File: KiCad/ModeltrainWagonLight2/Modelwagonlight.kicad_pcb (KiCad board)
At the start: 2 copper layers, 25 x 11 mm, 17 parts, among them J1 Conn_01x01, J2 Conn_01x01, J3 Conn_01x01, J4 Conn_01x01, U1 LP2951DR

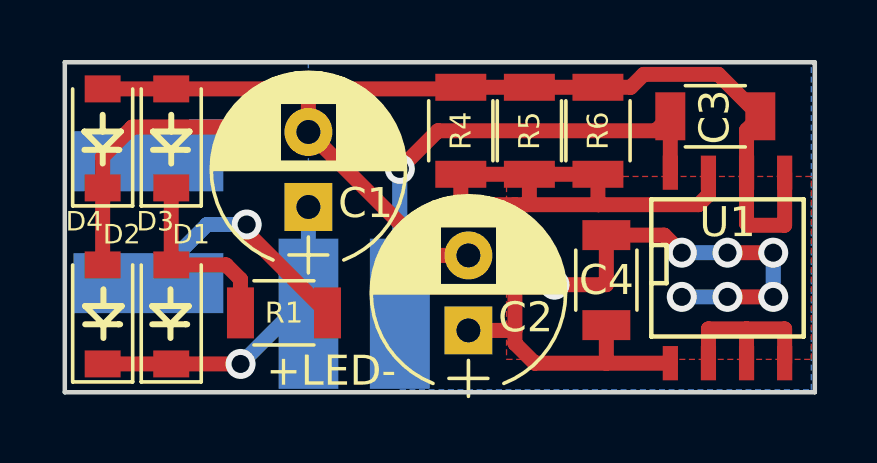
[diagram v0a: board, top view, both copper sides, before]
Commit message: Redrawn Modelwagonlight schematic and layout.
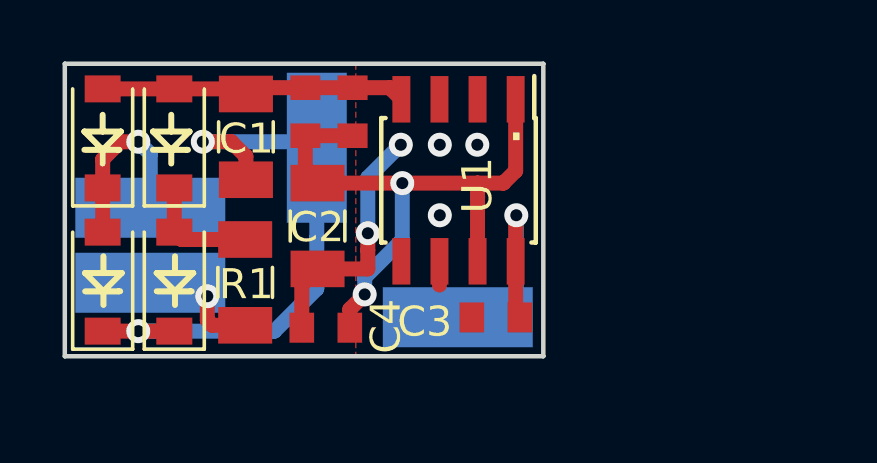
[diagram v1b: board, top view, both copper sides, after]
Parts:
- removed R6: 100R, Resistors_SMD:R_1206
- C1, C2: value 22uF -> 22u; footprint Capacitors_THT:CP_Radial_D6.3mm_P2.50mm -> Capacitor_SMD:C_1206_3216Metric
- C3, C4: value 100nF -> 100n; footprint Capacitors_SMD:C_1206 -> Capacitor_SMD:C_0603_1608Metric
- D1, D2: footprint Diodes_SMD:D_SOD-123 -> Diode_SMD:D_SOD-123
- R1: value 10R -> 47E; footprint Resistors_SMD:R_1206 -> Resistor_SMD:R_1206_3216Metric
- R4: value 100R -> 470E; footprint Resistors_SMD:R_1206 -> Resistor_SMD:R_0603_1608Metric
- R5: value 100R -> NP; footprint Resistors_SMD:R_1206 -> Resistor_SMD:R_0603_1608Metric
- U1: footprint SMD_Packages:SOIC-8-N -> Package_SO:SOIC-8_3.9x4.9mm_P1.27mm
- moved C3 9.92 mm to (204.4, 119.5), turned to 180 degrees
- moved C4 9.49 mm to (198.7, 119.8), turned to 180 degrees
- moved U1 9.43 mm to (203.1, 114.9), turned to 270 degrees
- moved C2 6.12 mm to (198.4, 116.5), turned to 270 degrees
- moved R5 5.93 mm to (199.6, 112.6)
- moved J3 5.54 mm to (198.4, 113.8)
- moved R4 5.22 mm to (198.0, 112.6)
- moved C1 3.13 mm to (196.0, 113.5)
- moved J4 1.94 mm to (203.1, 119.5), turned to 0 degrees
- moved R1 1.64 mm to (196.0, 118.3), turned to 90 degrees
- moved J2 1.55 mm to (192.8, 115.8), turned to 0 degrees
- moved D1 1.10 mm to (193.6, 118.3)
- moved D2 1.09 mm to (191.3, 118.3)
- moved D3 0.10 mm to (193.6, 113.5)
- moved J1 0.07 mm to (192.8, 118.3), turned to 0 degrees
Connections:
- net Net-(C1-Pad2) renamed GND
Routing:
- net GND: track 57.7 -> 19.6 mm, vias 7 -> 5
- net Net-(C2-Pad1): track 30.0 -> 20.7 mm, vias 0 -> 2
- net Net-(C1-Pad1): track 11.1 -> 19.9 mm
- net Net-(C3-Pad1): track 16.4 -> 8.82 mm
- net Net-(D2-Pad2): track 13.0 -> 6.22 mm
- net Net-(J1-Pad1): track 8.15 -> 4.22 mm
- net Net-(D1-Pad2): track 6.19 -> 3.94 mm
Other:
- board size 25 x 11 mm -> 15.9 x 9.8 mm
- board text added: "."
- board text added: "2019"
- board text added: "Jsif"
- board text added: "LED"
- board text added: "V2.0"
- board text added: "Wlight"
- board text added: "^IN^"
- board text removed: "+LED-"
- board text removed: "D1"
- board text removed: "D2"
- board text removed: "D3"
- board text removed: "D4"
- board text removed: "Jsif 2019 WagonLight"
- board text removed: "S"
